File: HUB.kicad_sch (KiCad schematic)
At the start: 4 parts, among them U14 CH334F, X1 X322512MSB4SI

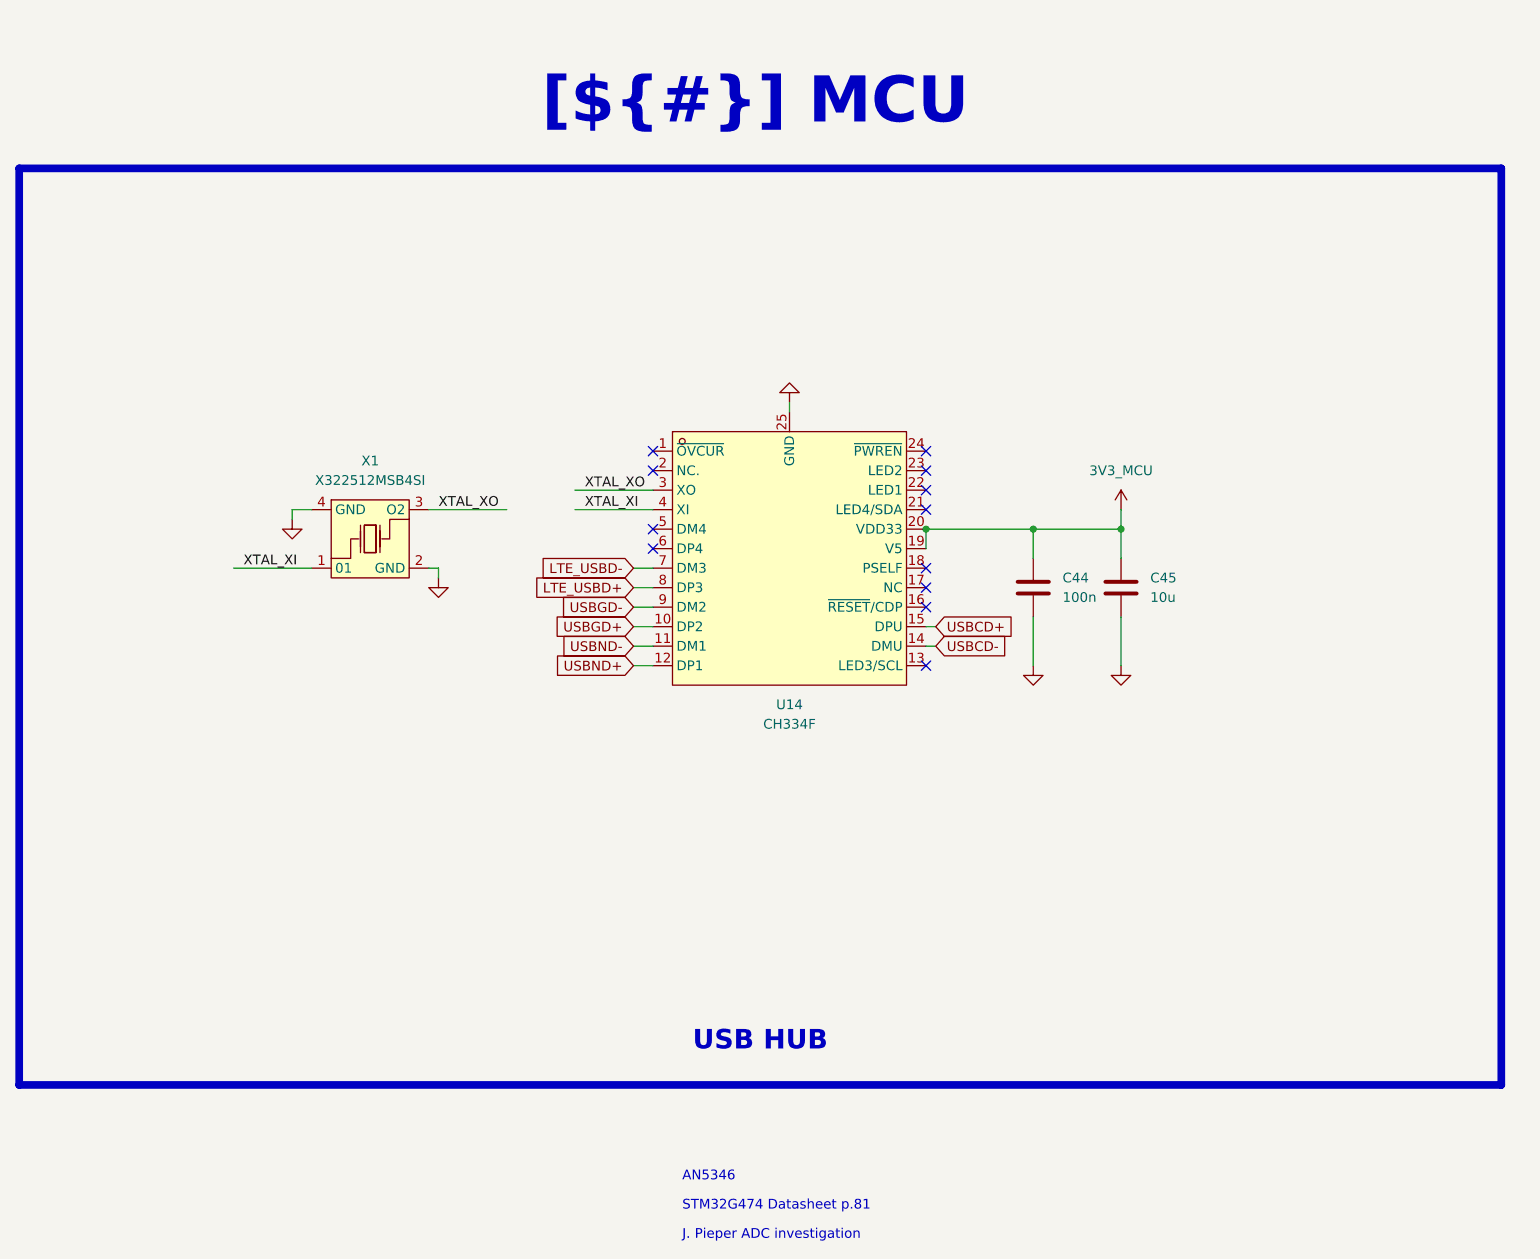
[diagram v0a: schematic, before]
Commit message: [Schematic][Added] Project Architecture, connectors
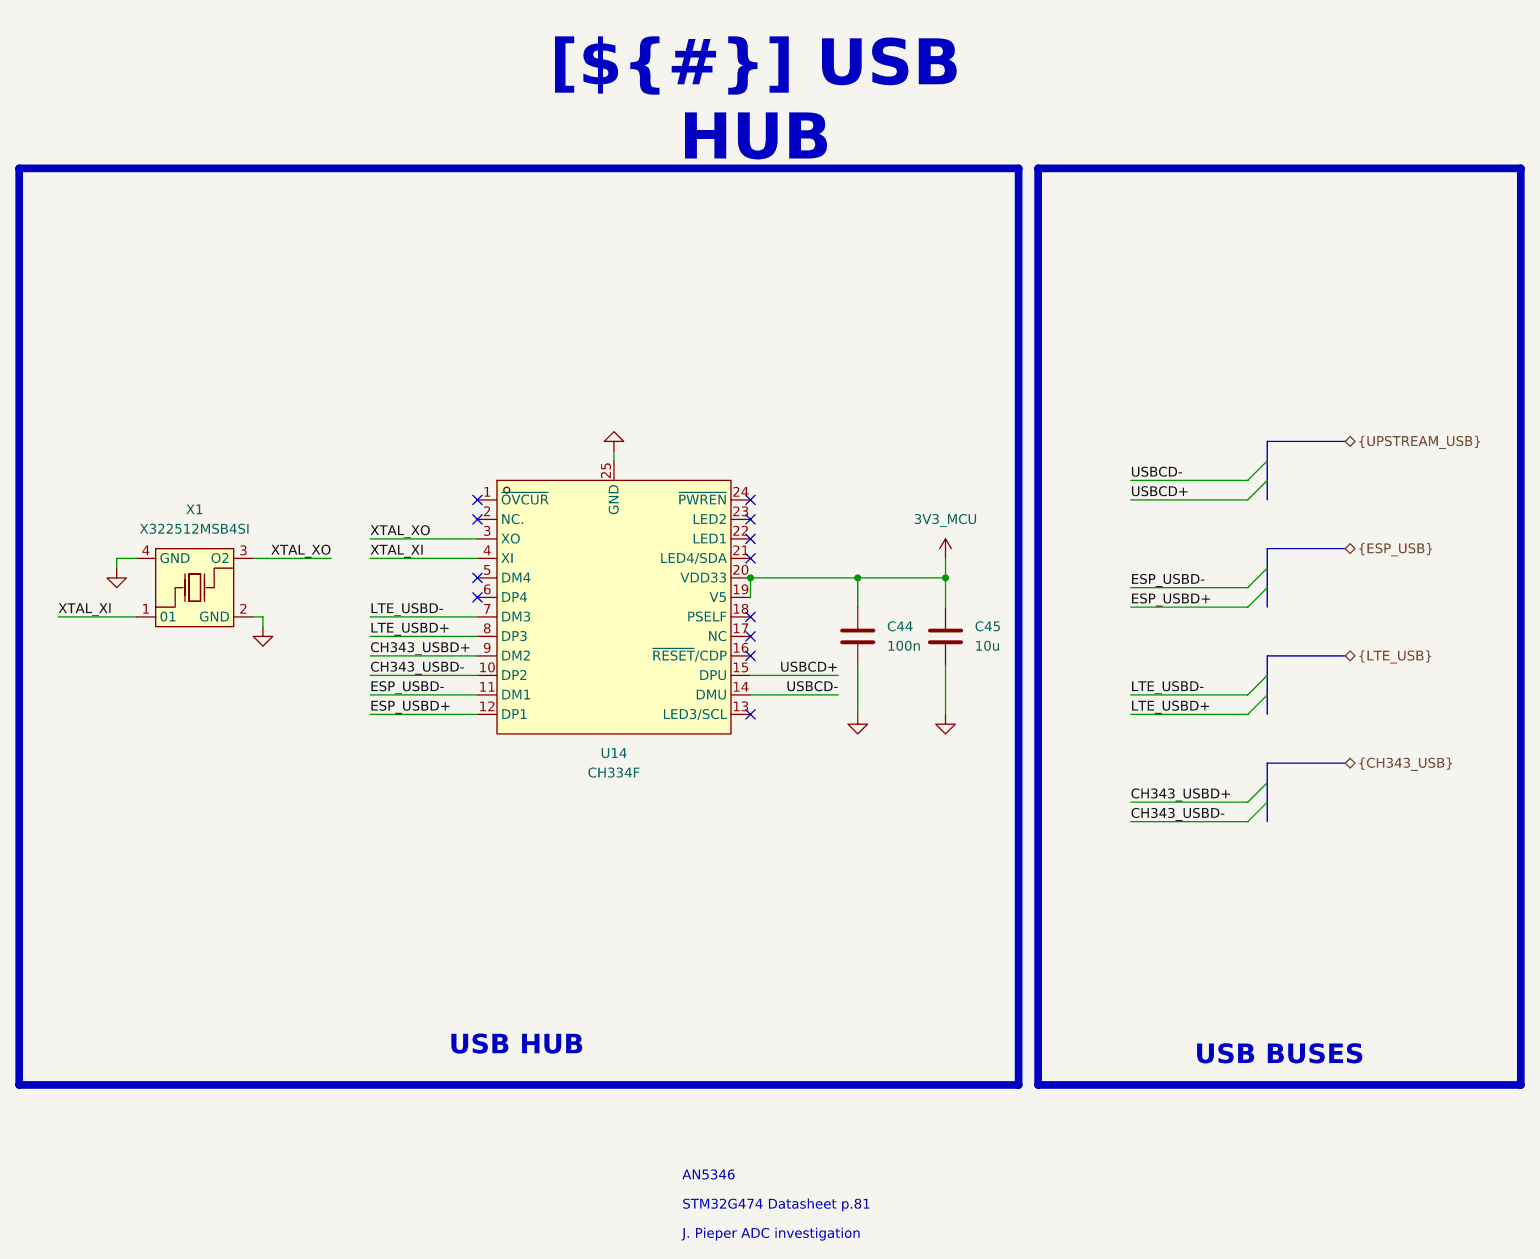
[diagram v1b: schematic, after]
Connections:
- net USBGD+ renamed CH343_USBD-
- net USBGD- renamed CH343_USBD+
- net USBND+ renamed ESP_USBD+
- net USBND- renamed ESP_USBD-
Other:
- title: MCU -> USB HUB
- moved on the sheet: C44, C45, U14, X1

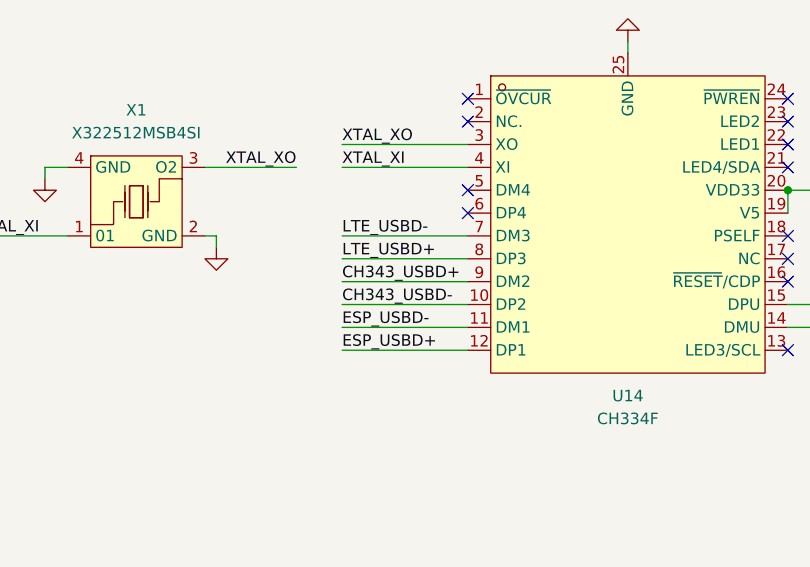
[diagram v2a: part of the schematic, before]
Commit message: [Schematic/PCB][Added] Connectors, layout, preliminar routing
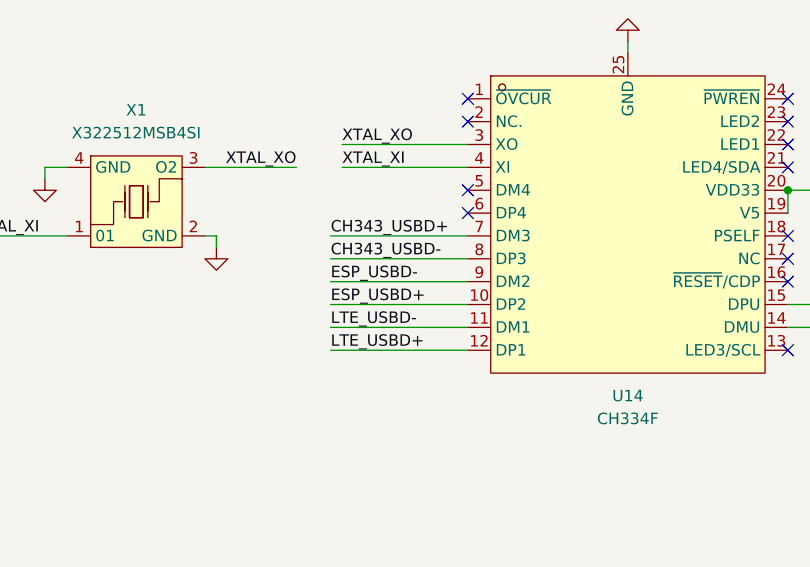
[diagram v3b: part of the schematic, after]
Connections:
- net CH343_USBD+: now also U14.7 (DM3); no longer U14.9 (DM2)
- net CH343_USBD-: now also U14.8 (DP3); no longer U14.10 (DP2)
- net ESP_USBD+: now also U14.10 (DP2); no longer U14.12 (DP1)
- net ESP_USBD-: now also U14.9 (DM2); no longer U14.11 (DM1)
- net LTE_USBD+: now also U14.12 (DP1); no longer U14.8 (DP3)
- net LTE_USBD-: now also U14.11 (DM1); no longer U14.7 (DM3)
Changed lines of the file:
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@@
+	(wire
+		(pts
+			(xy 100.33 93.98) (xy 115.57 93.98)
+		)
+		(stroke
+			(width 0)
+			(type default)
+		)
+	)
 	(wire
 		(pts
@@
 		)
 	)
+	(wire
+		(pts
+			(xy 100.33 96.52) (xy 115.57 96.52)
+		)
+		(stroke
+			(width 0)
+			(type default)
+		)
+	)
 	(bus
 		(pts
@@
 		)
 	)
+	(wire
+		(pts
+			(xy 100.33 99.06) (xy 115.57 99.06)
+		)
+		(stroke
+			(width 0)
+			(type default)
+		)
+	)
 	(bus
 		(pts
@@
 	(wire
 		(pts
-			(xy 101.6 99.06) (xy 115.57 99.06)
-		)
-		(stroke
-			(width 0)
-			(type default)
-		)
-	)
-	(wire
-		(pts
 			(xy 200.66 71.12) (xy 215.9 71.12)
 		)
@@
 	(wire
 		(pts
-			(xy 101.6 101.6) (xy 115.57 101.6)
-		)
-		(stroke
-			(width 0)
-			(type default)
-		)
-	)
-	(wire
-		(pts
-			(xy 101.6 88.9) (xy 115.57 88.9)
-		)
-		(stroke
-			(width 0)
-			(type default)
-		)
-	)
-	(wire
-		(pts
-			(xy 101.6 93.98) (xy 115.57 93.98)
+			(xy 100.33 101.6) (xy 115.57 101.6)
 		)
 		(stroke
@@
 	(wire
 		(pts
-			(xy 101.6 91.44) (xy 115.57 91.44)
-		)
-		(stroke
-			(width 0)
-			(type default)
-		)
-	)
-	(wire
-		(pts
-			(xy 101.6 96.52) (xy 115.57 96.52)
-		)
-		(stroke
-			(width 0)
-			(type default)
-		)
-	)
-	(wire
-		(pts
 			(xy 133.35 67.31) (xy 133.35 68.58)
 		)
@@
 	(wire
 		(pts
+			(xy 100.33 88.9) (xy 115.57 88.9)
+		)
+		(stroke
+			(width 0)
+			(type default)
+		)
+	)
+	(wire
+		(pts
 			(xy 86.36 81.28) (xy 96.52 81.28)
+		)
+		(stroke
+			(width 0)
+			(type default)
+		)
+	)
+	(wire
+		(pts
+			(xy 100.33 91.44) (xy 115.57 91.44)
 		)
 		(stroke
@@
 	)
 	(label "ESP_USBD-"
-		(at 101.6 99.06 0)
+		(at 100.33 93.98 0)
 		(effects
 			(font
@@
 	)
 	(label "CH343_USBD-"
-		(at 101.6 96.52 0)
+		(at 100.33 91.44 0)
 		(effects
 			(font
@@
 	)
 	(label "ESP_USBD+"
-		(at 101.6 101.6 0)
+		(at 100.33 96.52 0)
 		(effects
 			(font
@@
 	)
 	(label "CH343_USBD+"
-		(at 101.6 93.98 0)
+		(at 100.33 88.9 0)
 		(effects
 			(font
@@
 	)
 	(label "LTE_USBD-"
-		(at 101.6 88.9 0)
+		(at 100.33 99.06 0)
 		(effects
 			(font
@@
 	)
 	(label "LTE_USBD+"
-		(at 101.6 91.44 0)
-		(effects
-			(font
+		(at 100.33 101.6 0)
+		(effects
+			(font
